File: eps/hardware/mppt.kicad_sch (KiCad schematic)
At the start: 14 parts, among them U1 LTC3130IUDC_PBF

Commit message: add stm32 bsp and reconfigure pinout
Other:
- company: (none) -> SCRT
- title: (none) -> OSUSat CubeSat EPS
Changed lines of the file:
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@@
 	(generator_version "9.0")
 	(paper "A4")
+	(title_block
+		(title "OSUSat CubeSat EPS")
+		(date "2025-08-22")
+		(rev "1")
+		(company "SCRT")
+	)
 	(rectangle
 		(start 13.97 15.24)

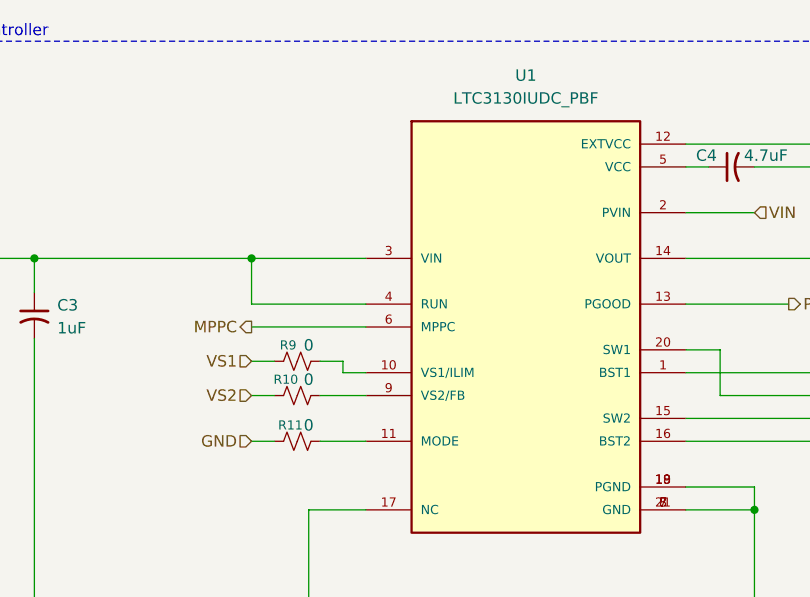
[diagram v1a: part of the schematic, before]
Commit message: fix ERC issues
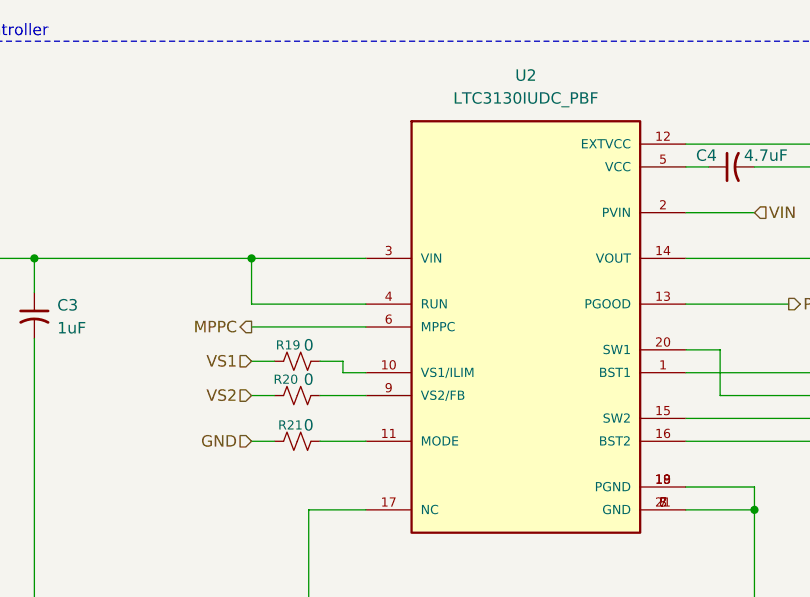
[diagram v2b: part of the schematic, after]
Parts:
- renumbered R9 to R19, R10 to R20, R11 to R21, U1 to U2
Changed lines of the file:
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@@
 		(dnp no)
 		(fields_autoplaced yes)
-		(property "Reference" "U1"
+		(property "Reference" "U2"
 			(at 101.6 19.05 0)
 			(effects
@@
 			(project ""
 				(path "/9e0ae2e7-d4be-41b4-8312-0d2aceea2180/fa2efaa0-4907-4b3e-94ec-ef462aa79480"
-					(reference "U1")
+					(reference "U2")
 					(unit 1)
 				)
@@
 		(on_board yes)
 		(dnp no)
-		(property "Reference" "R10"
+		(property "Reference" "R20"
 			(at 74.93 52.832 90)
 			(effects
@@
 			(project "eps"
 				(path "/9e0ae2e7-d4be-41b4-8312-0d2aceea2180/fa2efaa0-4907-4b3e-94ec-ef462aa79480"
-					(reference "R10")
+					(reference "R20")
 					(unit 1)
 				)
@@
 		(on_board yes)
 		(dnp no)
-		(property "Reference" "R11"
+		(property "Reference" "R21"
 			(at 75.438 57.912 90)
 			(effects
@@
 			(project ""
 				(path "/9e0ae2e7-d4be-41b4-8312-0d2aceea2180/fa2efaa0-4907-4b3e-94ec-ef462aa79480"
-					(reference "R11")
+					(reference "R21")
 					(unit 1)
 				)
@@
 		(dnp no)
 		(fields_autoplaced yes)
-		(property "Reference" "#FLG01"
+		(property "Reference" "#FLG02"
 			(at 24.13 33.655 0)
 			(effects
@@
 			(project ""
 				(path "/9e0ae2e7-d4be-41b4-8312-0d2aceea2180/fa2efaa0-4907-4b3e-94ec-ef462aa79480"
-					(reference "#FLG01")
+					(reference "#FLG02")
 					(unit 1)
 				)
@@
 		(on_board yes)
 		(dnp no)
-		(property "Reference" "R9"
+		(property "Reference" "R19"
 			(at 75.184 49.022 90)
 			(effects
@@
 			(project "eps"
 				(path "/9e0ae2e7-d4be-41b4-8312-0d2aceea2180/fa2efaa0-4907-4b3e-94ec-ef462aa79480"
-					(reference "R9")
+					(reference "R19")
 					(unit 1)
 				)

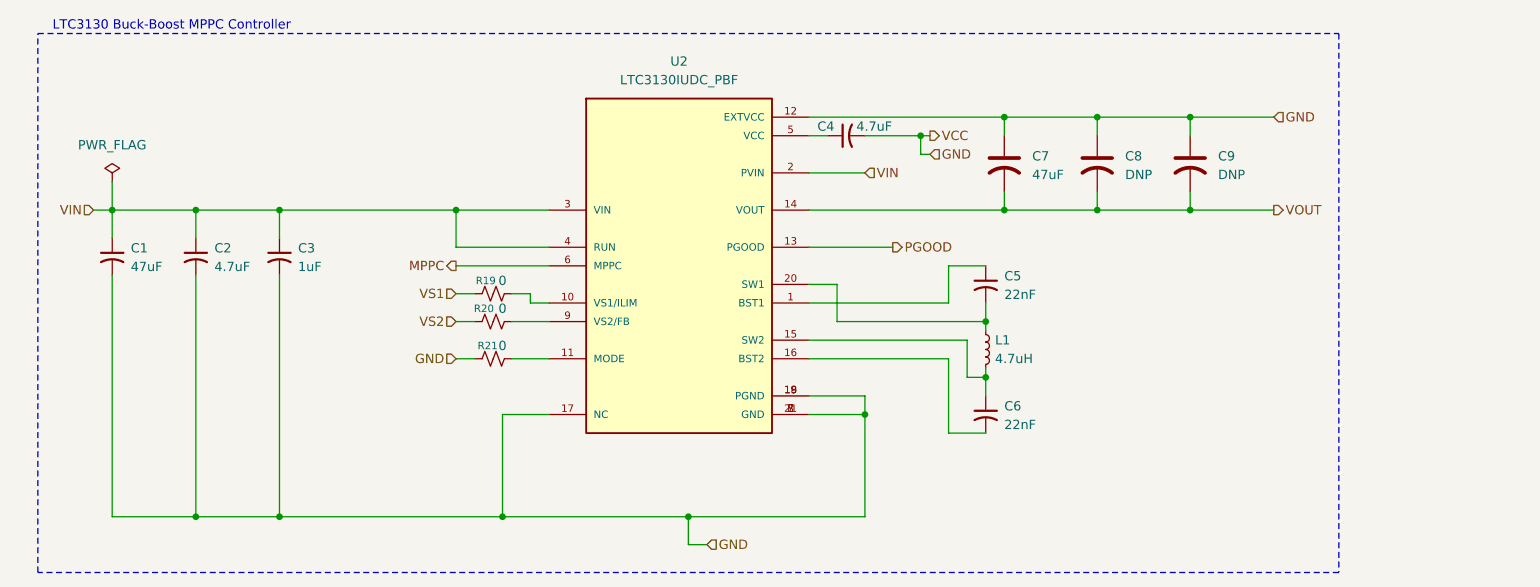
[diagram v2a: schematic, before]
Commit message: add ADC for MPPT sampling
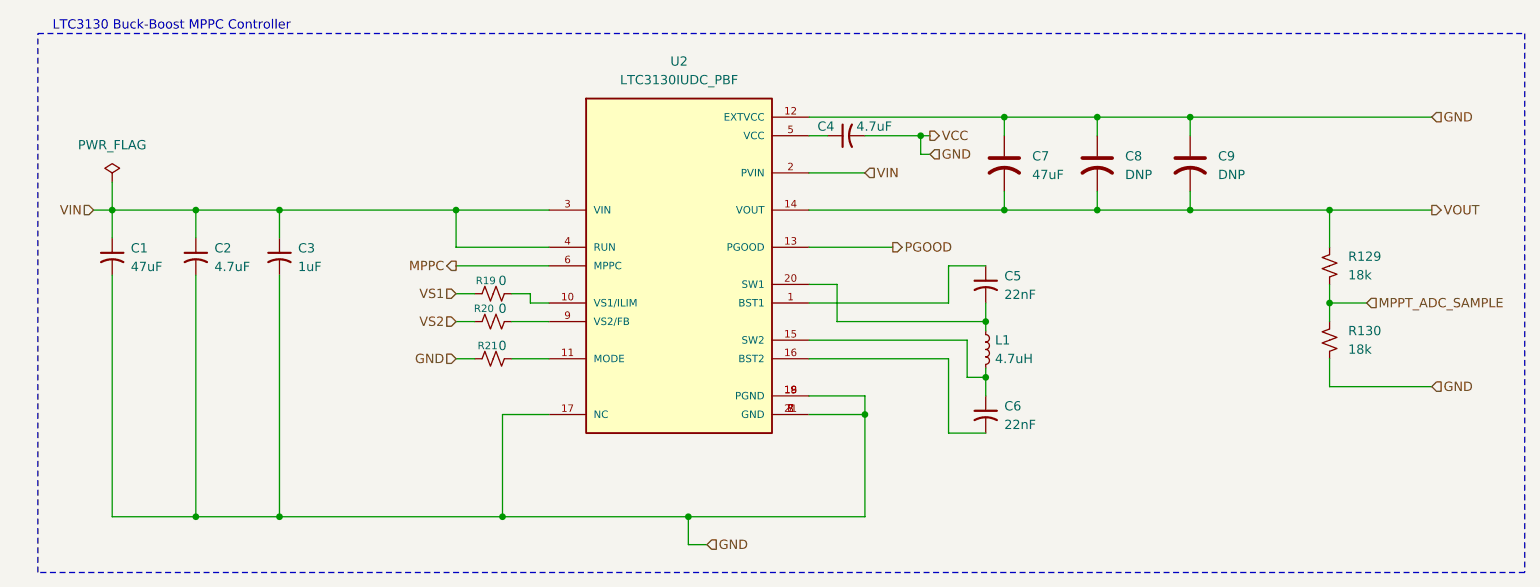
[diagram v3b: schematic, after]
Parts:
- added R129, R130: 18k, symbol Device:R_Small_US
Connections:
- net GND: now also R130.2
- net VOUT: now also R129.1
- new net MPPT_ADC_SAMPLE: R129.2, R130.1
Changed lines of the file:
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@@
 	(rectangle
 		(start 13.97 15.24)
-		(end 191.77 88.9)
+		(end 217.17 88.9)
 		(stroke
 			(width 0)
@@
 	)
 	(junction
+		(at 190.5 39.37)
+		(diameter 0)
+		(color 0 0 0 0)
+	)
+	(junction
+		(at 190.5 52.07)
+		(diameter 0)
+		(color 0 0 0 0)
+	)
+	(junction
 		(at 35.56 81.28)
 		(diameter 0)
@@
 	(wire
 		(pts
+			(xy 190.5 52.07) (xy 190.5 54.61)
+		)
+		(stroke
+			(width 0)
+			(type default)
+		)
+	)
+	(wire
+		(pts
 			(xy 119.38 34.29) (xy 127 34.29)
 		)
@@
 	(wire
 		(pts
+			(xy 190.5 52.07) (xy 195.58 52.07)
+		)
+		(stroke
+			(width 0)
+			(type default)
+		)
+	)
+	(wire
+		(pts
 			(xy 158.75 39.37) (xy 171.45 39.37)
 		)
@@
 	(wire
 		(pts
-			(xy 171.45 39.37) (xy 182.88 39.37)
+			(xy 171.45 39.37) (xy 190.5 39.37)
 		)
 		(stroke
@@
 	(wire
 		(pts
-			(xy 171.45 26.67) (xy 182.88 26.67)
+			(xy 171.45 26.67) (xy 204.47 26.67)
+		)
+		(stroke
+			(width 0)
+			(type default)
+		)
+	)
+	(wire
+		(pts
+			(xy 190.5 39.37) (xy 204.47 39.37)
 		)
 		(stroke
@@
 	(wire
 		(pts
+			(xy 190.5 49.53) (xy 190.5 52.07)
+		)
+		(stroke
+			(width 0)
+			(type default)
+		)
+	)
+	(wire
+		(pts
 			(xy 143.51 52.07) (xy 143.51 54.61)
 		)
@@
 	(wire
 		(pts
+			(xy 190.5 63.5) (xy 204.47 63.5)
+		)
+		(stroke
+			(width 0)
+			(type default)
+		)
+	)
+	(wire
+		(pts
 			(xy 77.47 67.31) (xy 77.47 81.28)
 		)
@@
 	(wire
 		(pts
+			(xy 190.5 39.37) (xy 190.5 44.45)
+		)
+		(stroke
+			(width 0)
+			(type default)
+		)
+	)
+	(wire
+		(pts
 			(xy 127 64.77) (xy 127 67.31)
 		)
@@
 		(pts
 			(xy 134.62 31.75) (xy 135.89 31.75)
+		)
+		(stroke
+			(width 0)
+			(type default)
+		)
+	)
+	(wire
+		(pts
+			(xy 190.5 59.69) (xy 190.5 63.5)
 		)
 		(stroke
@@
 	(hierarchical_label "GND"
 		(shape input)
+		(at 204.47 63.5 0)
+		(effects
+			(font
+				(size 1.27 1.27)
+			)
+			(justify left)
+		)
+	)
+	(hierarchical_label "GND"
+		(shape input)
 		(at 135.89 31.75 0)
 		(effects
@@
 	(hierarchical_label "VOUT"
 		(shape output)
-		(at 182.88 39.37 0)
+		(at 204.47 39.37 0)
 		(effects
 			(font
@@
 	(hierarchical_label "GND"
 		(shape input)
-		(at 182.88 26.67 0)
+		(at 204.47 26.67 0)
 		(effects
 			(font
@@
 			)
 			(justify right)
+		)
+	)
+	(hierarchical_label "MPPT_ADC_SAMPLE"
+		(shape input)
+		(at 195.58 52.07 0)
+		(effects
+			(font
+				(size 1.27 1.27)
+			)
+			(justify left)
 		)
 	)
@@
 	)
 	(symbol
+		(lib_id "Device:R_Small_US")
+		(at 190.5 57.15 0)
+		(mirror y)
+		(unit 1)
+		(exclude_from_sim no)
+		(in_bom yes)
+		(on_board yes)
+		(dnp no)
+		(property "Reference" "R130"
+			(at 193.04 55.8799 0)
+			(effects
+				(font
+					(size 1.27 1.27)
+				)
+				(justify right)
+			)
+		)
+		(property "Value" "18k"
+			(at 193.04 58.4199 0)
+			(effects
+				(font
+					(size 1.27 1.27)
+				)
+				(justify right)
+			)
+		)
+		(property "Footprint" ""
+			(at 190.5 57.15 0)
+			(effects
+				(font
+					(size 1.27 1.27)
+				)
+				(hide yes)
+			)
+		)
+		(property "Datasheet" "~"
+			(at 190.5 57.15 0)
+			(effects
+				(font
+					(size 1.27 1.27)
+				)
+				(hide yes)
+			)
+		)
+		(property "Description" "Resistor, small US symbol"
+			(at 190.5 57.15 0)
+			(effects
+				(font
+					(size 1.27 1.27)
+				)
+				(hide yes)
+			)
+		)
+		(pin "2"
+		)
+		(pin "1"
+		)
+		(instances
+			(project "eps"
+				(path "/9e0ae2e7-d4be-41b4-8312-0d2aceea2180/fa2efaa0-4907-4b3e-94ec-ef462aa79480"
+					(reference "R130")
+					(unit 1)
+				)
+			)
+		)
+	)
+	(symbol
 		(lib_id "Device:C_US")
 		(at 158.75 33.02 0)
@@
 					(unit 1)
 				)
+			)
+		)
+	)
+	(symbol
+		(lib_id "Device:R_Small_US")
+		(at 190.5 46.99 0)
+		(mirror y)
+		(unit 1)
+		(exclude_from_sim no)
+		(in_bom yes)
+		(on_board yes)
+		(dnp no)
+		(property "Reference" "R129"
+			(at 193.04 45.7199 0)
+			(effects
+				(font
+					(size 1.27 1.27)
+				)
+				(justify right)
+			)
+		)
+		(property "Value" "18k"
+			(at 193.04 48.2599 0)
+			(effects
+				(font
+					(size 1.27 1.27)
+				)
+				(justify right)
+			)
+		)
+		(property "Footprint" ""
+			(at 190.5 46.99 0)
+			(effects
+				(font
+					(size 1.27 1.27)
+				)
+				(hide yes)
+			)
+		)
+		(property "Datasheet" "~"
+			(at 190.5 46.99 0)
+			(effects
+				(font
+					(size 1.27 1.27)
+				)
+				(hide yes)
+			)
+		)
+		(property "Description" "Resistor, small US symbol"
+			(at 190.5 46.99 0)
+			(effects
+				(font
+					(size 1.27 1.27)
+				)
+				(hide yes)
+			)
+		)
+		(pin "2"
+		)
+		(pin "1"
+		)
+		(instances
+			(project ""
+				(path "/9e0ae2e7-d4be-41b4-8312-0d2aceea2180/fa2efaa0-4907-4b3e-94ec-ef462aa79480"
+					(reference "R129")
+					(unit 1)
+				)

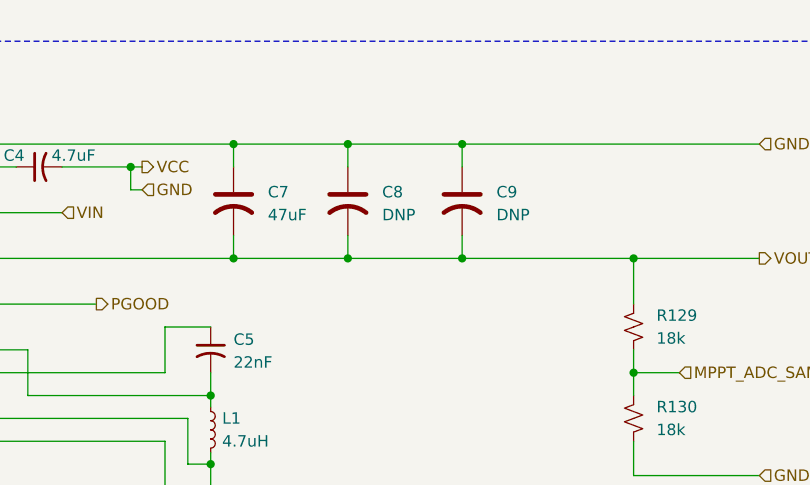
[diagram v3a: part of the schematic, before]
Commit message: fix erc issues
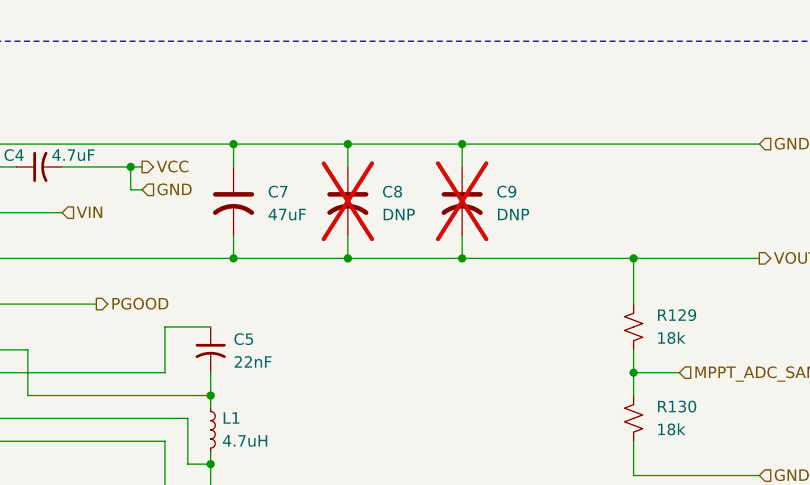
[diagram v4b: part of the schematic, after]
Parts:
- C8, C9: now not fitted
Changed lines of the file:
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@@
 		(in_bom yes)
 		(on_board yes)
-		(dnp no)
+		(dnp yes)
 		(fields_autoplaced yes)
 		(property "Reference" "C8"
@@
 		(in_bom yes)
 		(on_board yes)
-		(dnp no)
+		(dnp yes)
 		(fields_autoplaced yes)
 		(property "Reference" "C9"

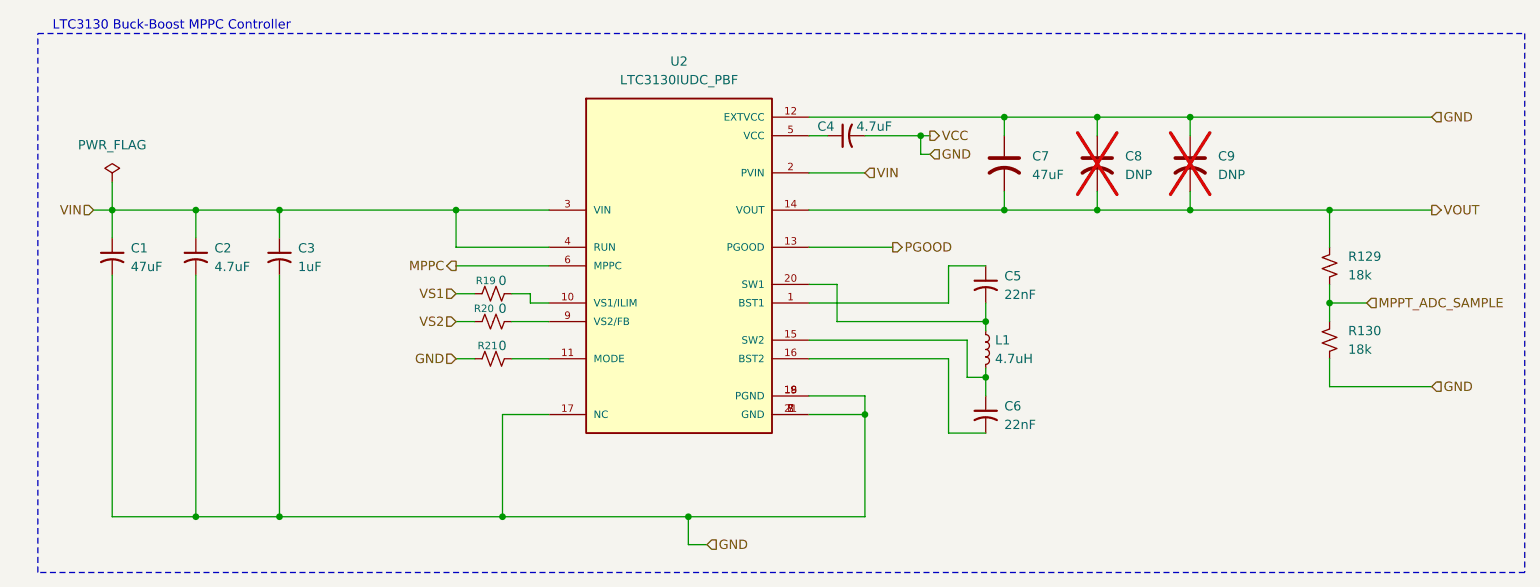
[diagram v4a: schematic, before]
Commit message: fix ERC issue in LTC3130-1
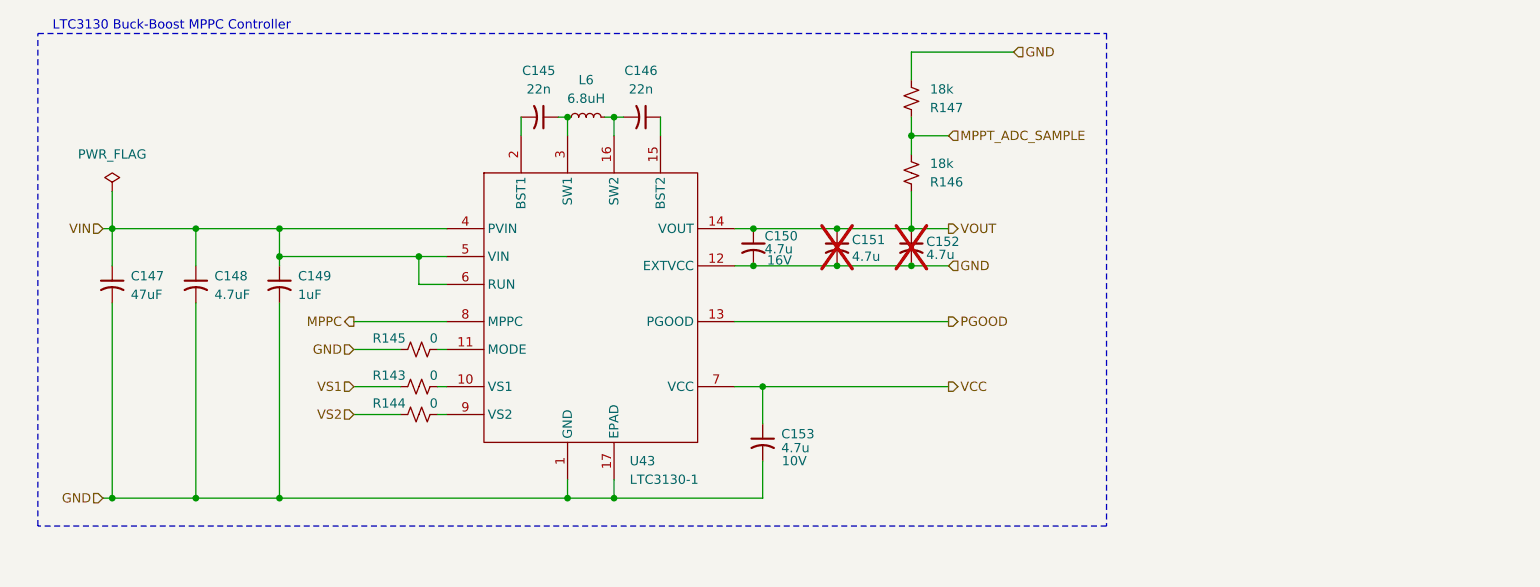
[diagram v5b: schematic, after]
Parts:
- removed C1: 47uF, symbol Device:C_Small_US
- removed C2, C4: 4.7uF, symbol Device:C_Small_US
- removed C3: 1uF, symbol Device:C_Small_US
- removed C5, C6: 22nF, symbol Device:C_Small_US
- removed C7: 47uF, symbol Device:C_US
- removed C8, C9: DNP, symbol Device:C_US
- removed L1: 4.7uH, symbol Device:L_Small
- removed R129, R130: 18k, symbol Device:R_Small_US
- removed R19, R20, R21: 0, symbol Device:R_Small_US
- removed U2: LTC3130IUDC_PBF, LTC3130IUDC_PBF:QFN50P400X300X80-21N, symbol LTC3130IUDC_PBF:LTC3130IUDC_PBF
- added C145, C146: 22n, symbol Device:C_Small_US
- added C147: 47uF, symbol Device:C_Small_US
- added C148: 4.7uF, symbol Device:C_Small_US
- added C149: 1uF, symbol Device:C_Small_US
- added C150, C151, C152, C153: 4.7u, symbol Device:C_Small_US
- added L6: 6.8uH, symbol Device:L_Small
- added R143, R144, R145: 0, symbol Device:R_Small_US
- added R146, R147: 18k, symbol Device:R_Small_US
- added U43: LTC3130-1, symbol EPS:LTC3130-1
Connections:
- net GND: now also C147.2, C148.2, C149.2, C150.2, C151.2, C152.2, C153.2, R145.1, R147.2, U43.1 (GND), U43.12 (EXTVCC), U43.17 (EPAD)
- net MPPC: now also U43.8 (MPPC)
- net MPPT_ADC_SAMPLE: now also R146.2, R147.1
- net PGOOD: now also U43.13 (PGOOD)
- net VIN: now also C147.1, C148.1, C149.1, U43.4 (PVIN), U43.5 (VIN), U43.6 (RUN)
- net VOUT: now also C150.1, C151.1, C152.1, R146.1, U43.14 (VOUT)
- net VS1: now also R143.1
- net VS2: now also R144.1
- new net: C146.1, U43.15 (BST2)
- new net: C146.2, L6.2, U43.16 (SW2)
- new net: C145.1, L6.1, U43.3 (SW1)
- new net: R143.2, U43.10 (VS1)
- new net: R145.2, U43.11 (MODE)
- new net: C145.2, U43.2 (BST1)
- new net: R144.2, U43.9 (VS2)
- new net VCC: C153.1, U43.7 (VCC)
